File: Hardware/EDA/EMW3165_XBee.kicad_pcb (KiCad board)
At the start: 2 copper layers, 24.4 x 27.6 mm, 8 parts, among them P1 XBEE P1-P10, P2 XBEE P11-P20, P3 JTAG, U1 EMW3165

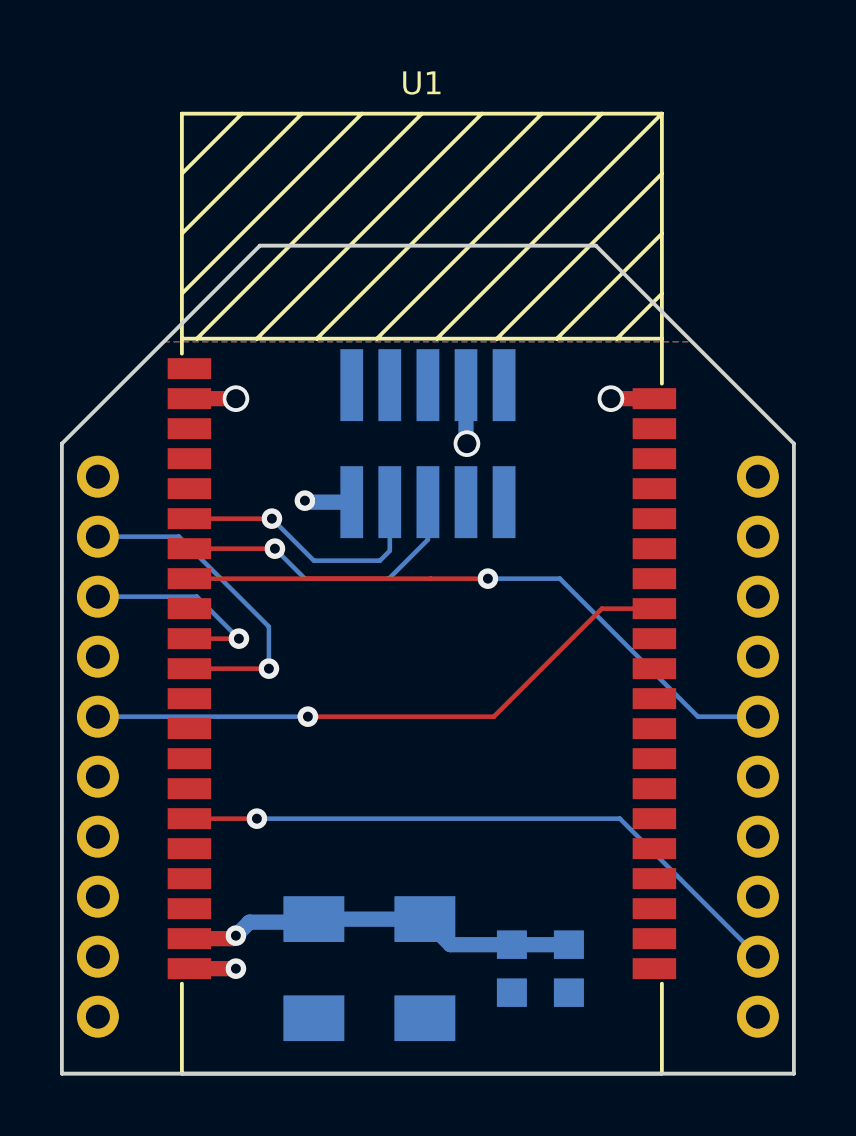
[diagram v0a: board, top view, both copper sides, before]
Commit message: Finished prototype design and generated gerbers for OSH Park.
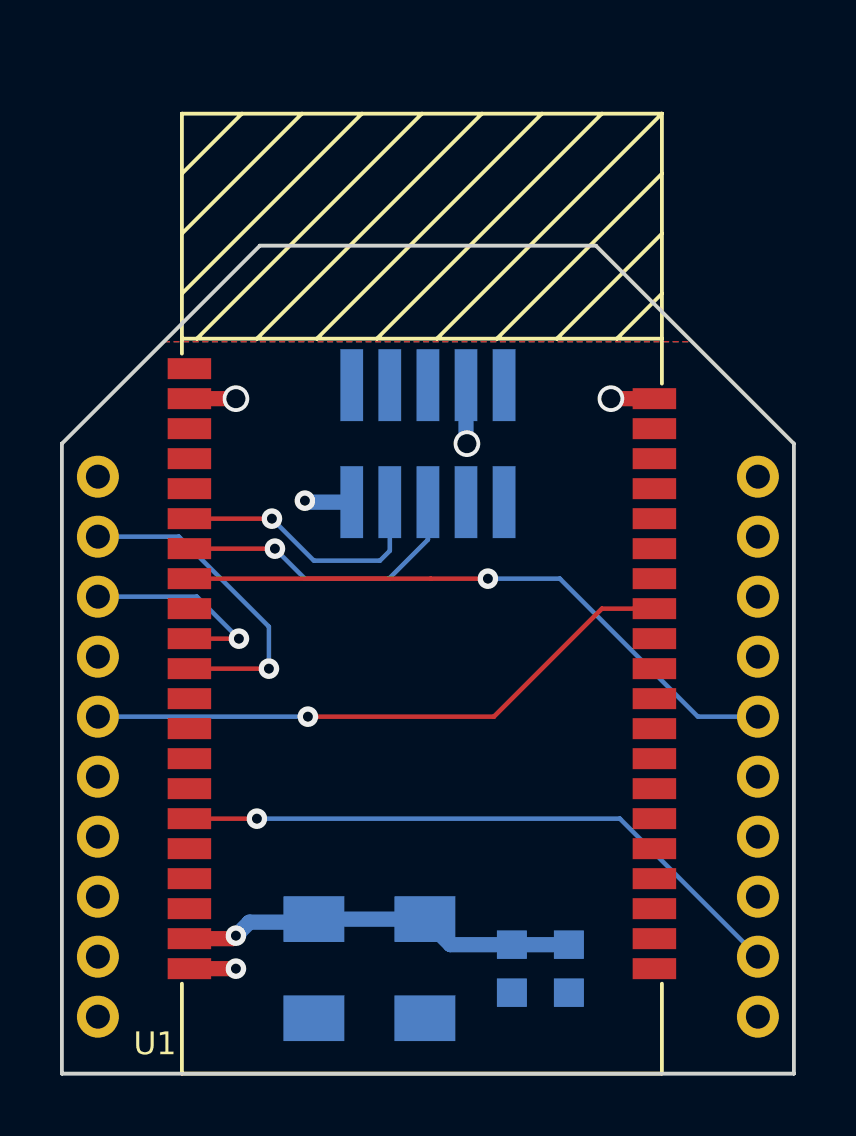
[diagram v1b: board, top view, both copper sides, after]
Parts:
- added G***: LOGO, Logo:Casco_Logix_Logo_4x4MM, B.Cu at (110.8, 90.0)
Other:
- board text added: "REV 0.1"
